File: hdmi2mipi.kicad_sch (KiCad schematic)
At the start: 168 parts, among them J10 BOOT, J11 USB_C_Receptacle_USB2.0, J2 HDMI_A_1.4, J4 TOUCH, J5 QWIIC, J7 SWD, J8 AudioJack3, J9 QWIIC, Q1 BC846, Q2 BC846, Q3 BC846, Q4 BC846, Q5 BC846, Q6 BC846, Q7 2SC2712, U1 RP2040, U2 W25Q16JVUXIQ, U3 SY6280AAC, U3 W25Q16JVUXIQ, U4 PCA9306DC, U4 SY8079AAC, U8 MS4344, X2 SG-210STF, Y1 12MHz

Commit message: Simplify and get ready for component placement and routing
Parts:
- removed C1, C15, C2: 22p, Capacitor_SMD:C_0402_1005Metric, symbol mch2021-rescue:C-Device
- removed C10, C11, C12, C13, C14, C4, C5, C6, C7: 100n, Capacitor_SMD:C_0402_1005Metric, symbol mch2021-rescue:C-Device
- removed C16, C17, C8: 22u, Capacitor_SMD:C_0805_2012Metric, symbol mch2021-rescue:C-Device
- removed C3, C9: 1u, Capacitor_SMD:C_0402_1005Metric, symbol mch2021-rescue:C-Device
- removed C53: 2.2u, Capacitor_SMD:C_0402_1005Metric, symbol Device:C_Small
- removed C54: ~, Capacitor_SMD:C_0402_1005Metric, symbol Device:C_Small
- removed D2, D3, D4, D5: LED, LED_SMD:LED_0603_1608Metric, symbol Device:LED
- removed D5: D, symbol Device:D
- removed J10: BOOT, Connector_PinHeader_2.54mm:PinHeader_1x02_P2.54mm_Vertical, symbol Connector_Generic:Conn_01x02
- removed J11: USB_C_Receptacle_USB2.0, Connector_USB:USB_C_Receptacle_HRO_TYPE-C-31-M-12, symbol Connector:USB_C_Receptacle_USB2.0
- removed J4: TOUCH, Connector_JST:JST_SH_SM07B-SRSS-TB_1x07-1MP_P1.00mm_Horizontal, symbol Connector_Generic_MountingPin:Conn_01x07_MountingPin
- removed J5: QWIIC, Connector_JST:JST_SH_SM04B-SRSS-TB_1x04-1MP_P1.00mm_Horizontal, symbol Connector_Generic_MountingPin:Conn_01x04_MountingPin
- removed J7: SWD, Connector_JST:JST_SH_SM03B-SRSS-TB_1x03-1MP_P1.00mm_Horizontal, symbol Connector_Generic_MountingPin:Conn_01x03_MountingPin
- removed L1: 2.2u, custom:Inductor_MSC20FC, symbol mch2021-rescue:L-Device
- removed L5: ~, symbol mch2021-rescue:L-Device
- removed R1, R50: 10k, Resistor_SMD:R_0402_1005Metric, symbol Device:R_Small
- removed R14, R15: 5.1k, Resistor_SMD:R_0402_1005Metric, symbol mch2021-rescue:R-Device
- removed R16 (x4): 10k, Resistor_SMD:R_0402_1005Metric, symbol mch2021-rescue:R-Device
- removed R17: 45.3k, Resistor_SMD:R_0402_1005Metric, symbol mch2021-rescue:R-Device
- removed R18, R5, R8: 1k, Resistor_SMD:R_0402_1005Metric, symbol mch2021-rescue:R-Device
- removed R2: 0, Resistor_SMD:R_0402_1005Metric, symbol mch2021-rescue:R-Device
- removed R23, R24, R25, R26, R28: 4.7k, Resistor_SMD:R_0402_1005Metric, symbol Device:R_Small
- removed R3, R4: 10, Resistor_SMD:R_0402_1005Metric, symbol mch2021-rescue:R-Device
- removed R5: 6.8k, Resistor_SMD:R_0402_1005Metric, symbol mch2021-rescue:R-Device
- removed R5 (x2): 100, Resistor_SMD:R_0402_1005Metric, symbol mch2021-rescue:R-Device
- removed R6, R7: 27, Resistor_SMD:R_0402_1005Metric, symbol mch2021-rescue:R_Small-Device
- removed R63: 47k, Resistor_SMD:R_0402_1005Metric, symbol mch2021-rescue:R-Device
- removed R64: 100k, Resistor_SMD:R_0402_1005Metric, symbol mch2021-rescue:R-Device
- removed RN1: 1K, Resistor_SMD:R_Array_Convex_4x0402, symbol Device:R_Pack04
- removed TP1, TP2, TP3: TestPoint, TestPoint:TestPoint_Pad_D1.0mm, symbol Connector:TestPoint
- removed TP4, TP5: TestPoint, TestPoint:TestPoint_Pad_D2.0mm, symbol Connector:TestPoint
- removed U1: RP2040, custom:QFN40P700X700X90-57N, symbol RP2040:RP2040
- removed U12: ~, Package_TO_SOT_SMD:SOT-23-6, symbol lp3382s:LP3382S
- removed U2: W25Q16JVUXIQ, custom:PSON50P300X200X60-9N, symbol mch2021-rescue:SPIFLASH_QSPI-spiflash
- removed U3: W25Q16JVUXIQ, Package_SO:SOIC-8_5.23x5.23mm_P1.27mm, symbol mch2021-rescue:SPIFLASH_QSPI-spiflash
- removed U3: SY6280AAC, Package_TO_SOT_SMD:SOT-23-5, symbol symbols:AAT4610BIGV-1-T1-Power_Management
- removed U4: PCA9306DC, Package_SO:VSSOP-8_2.3x2mm_P0.5mm, symbol Interface:PCA9306DC
- removed U4: SY8079AAC, Package_TO_SOT_SMD:SOT-23-5, symbol mch2021-rescue:TLV62568DBV-Regulator_Switching
- removed Y1: 12MHz, Crystal:Crystal_SMD_3225-4Pin_3.2x2.5mm, symbol mch2021-rescue:Crystal_GND24_Small-Device
- added J1: IO, Connector_PinHeader_2.54mm:PinHeader_2x06_P2.54mm_Vertical, symbol Connector_Generic:Conn_02x06_Odd_Even
- added J4, J5: Conn_01x04, Connector_PinHeader_2.54mm:PinHeader_1x04_P2.54mm_Vertical, symbol Connector_Generic:Conn_01x04
- added J6: Conn_01x03, Connector_PinHeader_2.54mm:PinHeader_1x04_P2.54mm_Vertical, symbol Connector_Generic:Conn_01x03
- C6: value ~ -> 0.1u
- H1, H2, H3, H4: LCSC (none) -> -
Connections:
- net 1V1_EN is gone; now on net +3V3: U4.1 (EN)
- net 1V2_EN is gone; now on net +3V3: U4.1 (EN)
- net 1V8_EN is gone; now on net +3V3: U4.1 (EN)
- net VBUS is gone; now on net +3V3: C6.1, C6.1, C6.1, C8.1, C8.1, C8.1, U4.4 (VIN), U4.4 (VIN), U4.4 (VIN)
- net VDD33_HDMI is gone; now on net +3V3: C6.1, C6.1, C8.1, J3.24 (3.3v), J3.25 (3.3v), Q7.3 (C), R10.2, R27.1, R29.1, R41.1, R43.1, U2.B1 (VDD33_HDMI), U2.G1 (VDD33_HDMI), U2.H2 (VDDIO33), U2.J7 (VDDIO18), X2.1 (~{ST}), X2.4 (Vcc)
- net +1V1: now also J4.2 (Pin_2)
- net +1V2: now also J4.3 (Pin_3)
- net +1V8: now also J4.4 (Pin_4)
- net +3V3: now also R38.1, J1.11 (Pin_11), J5.2 (Pin_2)
- net 1V8_S1: now also J1.3 (Pin_3)
- net 1V8_S2: now also J1.5 (Pin_5)
- net 3V3_S1: now also J1.7 (Pin_7)
- net 3V3_S2: now also J1.9 (Pin_9)
- net GND: now also J1.1 (Pin_1), J1.2 (Pin_2), J4.1 (Pin_1), J5.1 (Pin_1), J6.3 (Pin_3); no longer R38.2
- net at R40.1, U2.J3 (INT): now also J6.1 (Pin_1)
- net at J9.3 (Pin_3), R29.2, U2.K3 (I2C_SDA): now also J5.3 (Pin_3)
- net at J9.4 (Pin_4), R27.2, U2.K4 (I2C_SCL): now also J5.4 (Pin_4)
- net at U2.K8 (~{RESET}): now also R38.2, J6.2 (Pin_2); no longer R38.1
- net at J3.5 (FB2), J3.6 (FB2): now also J1.6 (Pin_6)
- net at J3.1 (FB1), J3.2 (FB1): now also J1.4 (Pin_4)
- net at J3.14 (5.8v-VDD): now also J1.12 (Pin_12)
- net at J3.10 (LED+), J3.8 (LED+), J3.9 (LED+): now also J1.8 (Pin_8)
- net at J3.13 (5.8v-VEE): now also J1.10 (Pin_10)
- no-connect marks 14 -> 12
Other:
- note removed: "I2C0 SDA I2C0 SCL"
- note removed: "I2C1 SDA I2C1 SCL"
- note removed: "Place close to chip"
- note removed: "Place close to pin 44"
- note removed: "Place close to pin 45"
- note removed: "SPI0 SCK SPI0 TX SPI0 RX"
- note removed: "SPI1 SCK SPI1 TX SPI1 RX"
- note removed: "UART0 TX UART0 RX UART0 CTS UART0 RTS"
- note removed: "UART1 TX UART1 RX UART1 CTS UART1 RTS"
- company: Nicolai Electronics -> Nicolai Electronics & Badge.Team
- title: HDMI to MIPI converter -> HDMI to MIPI converter (simplified)
- moved on the sheet: R38

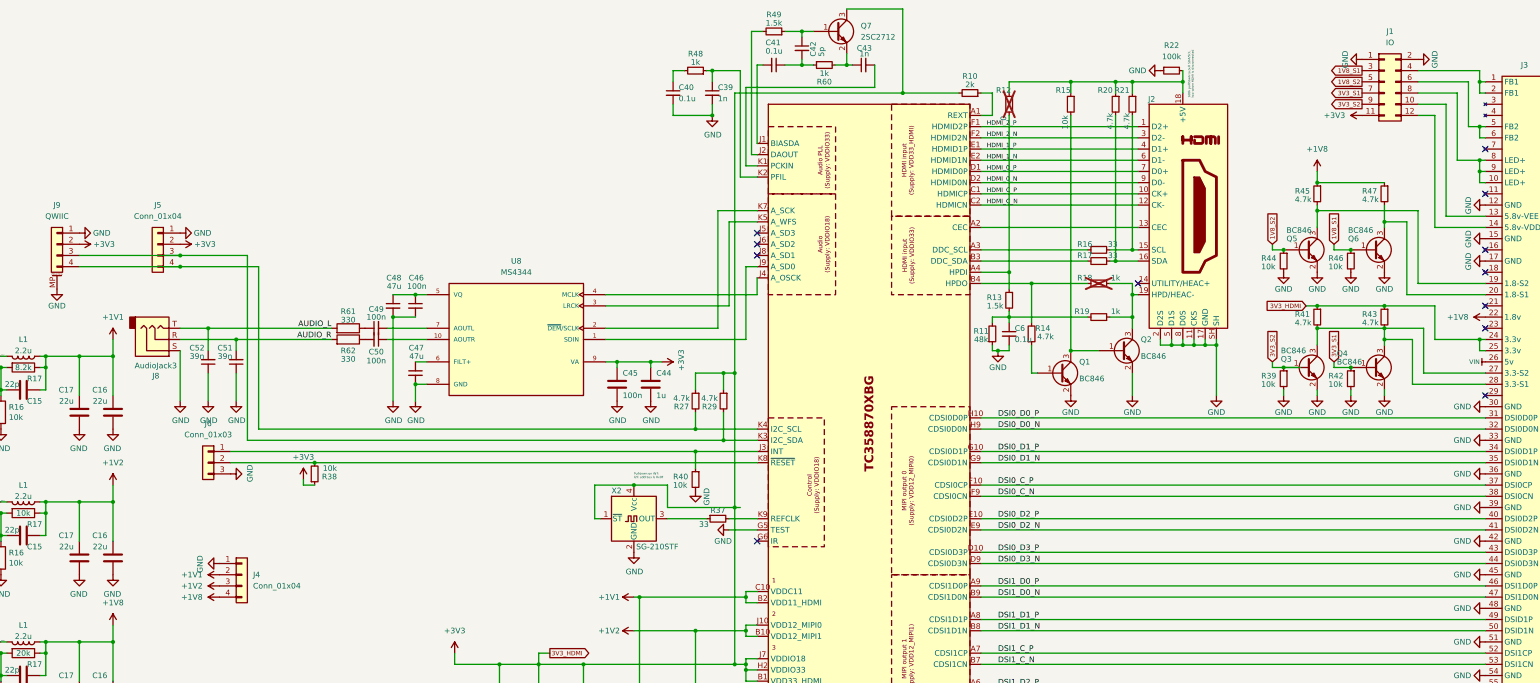
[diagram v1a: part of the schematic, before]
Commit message: Small fixes and combine 2.54mm headers
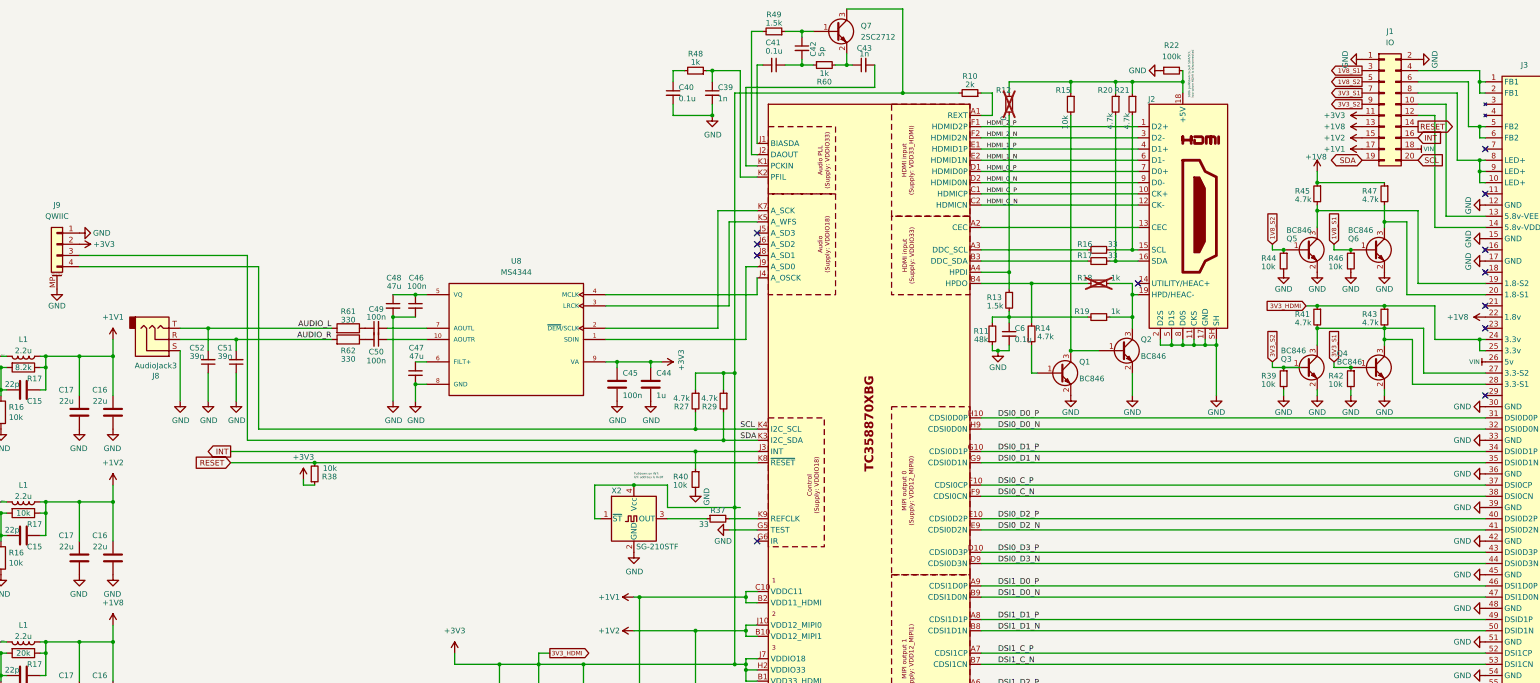
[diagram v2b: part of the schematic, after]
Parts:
- removed J4, J5: Conn_01x04, Connector_PinHeader_2.54mm:PinHeader_1x04_P2.54mm_Vertical, symbol Connector_Generic:Conn_01x04
- removed J6: Conn_01x03, Connector_PinHeader_2.54mm:PinHeader_1x04_P2.54mm_Vertical, symbol Connector_Generic:Conn_01x03
- J1: footprint Connector_PinHeader_2.54mm:PinHeader_2x06_P2.54mm_Vertical -> Connector_PinHeader_2.54mm:PinHeader_2x10_P2.54mm_Vertical; symbol Connector_Generic:Conn_02x06_Odd_Even -> Connector_Generic:Conn_02x10_Odd_Even
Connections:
- net +1V1: now also J1.17 (Pin_17)
- net +1V2: now also J1.15 (Pin_15)
- net +1V8: now also J1.13 (Pin_13)
- net VIN: now also J1.18 (Pin_18)
- net INT: now reaches R40.1, U2.J3 (INT)
- net INT: now also J1.16 (Pin_16)
- net SDA: now reaches J9.3 (Pin_3), R29.2, U2.K3 (I2C_SDA)
- net SDA: now also J1.19 (Pin_19)
- net SCL: now reaches J9.4 (Pin_4), R27.2, U2.K4 (I2C_SCL)
- net SCL: now also J1.20 (Pin_20)
- net RESET: now reaches R38.2, U2.K8 (~{RESET})
- net RESET: now also J1.14 (Pin_14)

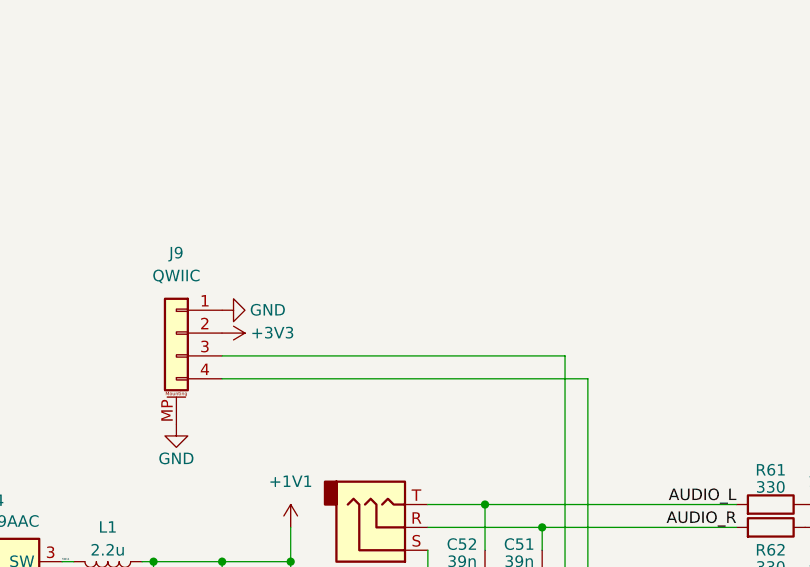
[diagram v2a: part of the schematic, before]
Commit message: Changed copper layers, heaps of other issues.
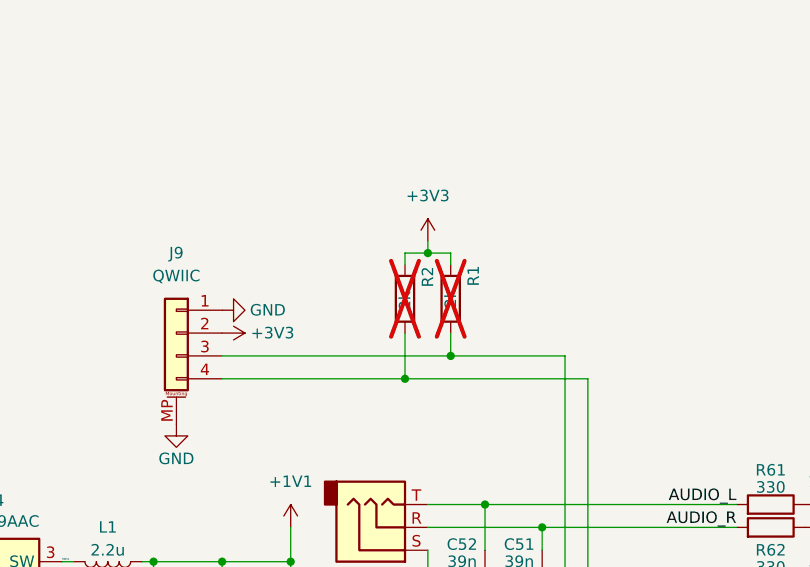
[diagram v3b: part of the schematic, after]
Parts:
- added R1, R2: 2k, Resistor_SMD:R_0402_1005Metric, symbol mch2021-rescue:R-Device
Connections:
- net +3V3: now also R1.1, R2.1
- net SCL: now also R2.2
- net SDA: now also R1.2

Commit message: Last tweaks and order at JLC
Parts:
- C39, C43: LCSC (none) -> C527013
- C40, C41, C6: LCSC (none) -> C106256
- C42: LCSC (none) -> C359289
- H1, H2, H3, H4: now not fitted
- J1: LCSC (none) -> -; now not fitted
- J2: LCSC (none) -> C720616
- J3: LCSC (none) -> C224193
- J9: LCSC (none) -> C160404
- Q1, Q2, Q3, Q4, Q5, Q6: LCSC (none) -> C181138
- Q7: LCSC (none) -> C83447
- R10: LCSC (none) -> C25744
- R11: value 48k -> 47k; LCSC (none) -> C380748
- R12: LCSC (none) -> -
- R13, R49: LCSC (none) -> C409724
- U2: LCSC (none) -> C3008712
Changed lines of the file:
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@@
 	(title_block
 		(title "HDMI to MIPI converter (simplified)")
-		(date "2024-02-21")
+		(date "2024-03-29")
 		(rev "0.1")
 		(company "Nicolai Electronics & Badge.Team")
@@
 			)
 		)
+		(property "LCSC" "C3008712"
+			(at 254 175.26 0)
+			(effects
+				(font
+					(size 1.27 1.27)
+				)
+				(hide yes)
+			)
+		)
 		(pin "H10"
 		)
@@
 		(in_bom yes)
 		(on_board yes)
-		(dnp no)
+		(dnp yes)
 		(fields_autoplaced yes)
 		(property "Reference" "J1"
@@
 			)
 		)
+		(property "LCSC" "-"
+			(at 370.84 102.87 0)
+			(effects
+				(font
+					(size 1.27 1.27)
+				)
+				(hide yes)
+			)
+		)
 		(pin "6"
 		)
@@
 			)
 		)
+		(property "LCSC" "C409724"
+			(at 232.41 86.36 0)
+			(effects
+				(font
+					(size 1.27 1.27)
+				)
+				(hide yes)
+			)
+		)
 		(pin "2"
 		)
@@
 			)
 		)
+		(property "LCSC" "C181138"
+			(at 311.15 158.75 0)
+			(effects
+				(font
+					(size 1.27 1.27)
+				)
+				(hide yes)
+			)
+		)
 		(pin "1"
 		)
@@
 			)
 		)
+		(property "LCSC" "C181138"
+			(at 297.18 163.83 0)
+			(effects
+				(font
+					(size 1.27 1.27)
+				)
+				(hide yes)
+			)
+		)
 		(pin "1"
 		)
@@
 			)
 		)
-		(property "Value" "48k"
+		(property "Value" "47k"
 			(at 279.4 156.21 0)
 			(effects
@@
 			)
 		)
+		(property "LCSC" "C380748"
+			(at 281.94 154.94 0)
+			(effects
+				(font
+					(size 1.27 1.27)
+				)
+				(hide yes)
+			)
+		)
 		(pin "2"
 		)
@@
 			)
 		)
+		(property "LCSC" "C83447"
+			(at 246.38 86.36 0)
+			(effects
+				(font
+					(size 1.27 1.27)
+				)
+				(hide yes)
+			)
+		)
 		(pin "1"
 		)
@@
 			)
 		)
+		(property "LCSC" "C25744"
+			(at 276.86 100.33 0)
+			(effects
+				(font
+					(size 1.27 1.27)
+				)
+				(hide yes)
+			)
+		)
 		(pin "2"
 		)
@@
 			)
 		)
+		(property "LCSC" "C527013"
+			(at 252.73 93.98 0)
+			(effects
+				(font
+					(size 1.27 1.27)
+				)
+				(hide yes)
+			)
+		)
 		(pin "2"
 		)
@@
 			)
 		)
+		(property "LCSC" "C181138"
+			(at 368.3 135.89 0)
+			(effects
+				(font
+					(size 1.27 1.27)
+				)
+				(hide yes)
+			)
+		)
 		(pin "3"
 		)
@@
 			)
 		)
+		(property "LCSC" "C160404"
+			(at 69.85 134.62 0)
+			(effects
+				(font
+					(size 1.27 1.27)
+				)
+				(hide yes)
+			)
+		)
 		(pin "2"
 		)
@@
 			)
 		)
+		(property "LCSC" "C359289"
+			(at 238.76 90.17 0)
+			(effects
+				(font
+					(size 1.27 1.27)
+				)
+				(hide yes)
+			)
+		)
 		(pin "2"
 		)
@@
 			)
 		)
+		(property "LCSC" "C106256"
+			(at 285.75 154.94 0)
+			(effects
+				(font
+					(size 1.27 1.27)
+				)
+				(hide yes)
+			)
+		)
 		(pin "2"
 		)
@@
 		(in_bom yes)
 		(on_board yes)
-		(dnp no)
+		(dnp yes)
 		(property "Reference" "H2"
 			(at 276.86 264.795 0)
@@
 		(in_bom yes)
 		(on_board yes)
-		(dnp no)
+		(dnp yes)
 		(property "Reference" "H3"
 			(at 281.94 264.795 0)
@@
 			)
 		)
+		(property "LCSC" "C106256"
+			(at 232.41 93.98 0)
+			(effects
+				(font
+					(size 1.27 1.27)
+				)
+				(hide yes)
+			)
+		)
 		(pin "2"
 		)
@@
 			)
 		)
+		(property "LCSC" "C224193"
+			(at 398.78 173.99 0)
+			(effects
+				(font
+					(size 1.27 1.27)
+				)
+				(hide yes)
+			)
+		)
 		(pin "34"
 		)
@@
 			)
 		)
+		(property "LCSC" "C720616"
+			(at 325.12 128.27 0)
+			(effects
+				(font
+					(size 1.27 1.27)
+				)
+				(hide yes)
+			)
+		)
 		(pin "7"
 		)
@@
 			)
 		)
+		(property "LCSC" "C527013"
+			(at 218.44 100.33 0)
+			(effects
+				(font
+					(size 1.27 1.27)
+				)
+				(hide yes)
+			)
+		)
 		(pin "2"
 		)
@@
 		(in_bom yes)
 		(on_board yes)
-		(dnp no)
+		(dnp yes)
 		(property "Reference" "H1"
 			(at 271.78 264.795 0)
@@
 			)
 		)
+		(property "LCSC" "C181138"
+			(at 353.06 162.56 0)
+			(effects
+				(font
+					(size 1.27 1.27)
+				)
+				(hide yes)
+			)
+		)
 		(pin "3"
 		)
@@
 			)
 		)
+		(property "LCSC" "C409724"
+			(at 285.75 147.32 0)
+			(effects
+				(font
+					(size 1.27 1.27)
+				)
+				(hide yes)
+			)
+		)
 		(pin "2"
 		)
@@
 		(in_bom yes)
 		(on_board yes)
-		(dnp no)
+		(dnp yes)
 		(property "Reference" "H4"
 			(at 287.02 264.795 0)
@@
 			)
 		)
+		(property "LCSC" "C181138"
+			(at 368.3 162.56 0)
+			(effects
+				(font
+					(size 1.27 1.27)
+				)
+				(hide yes)
+			)
+		)
 		(pin "3"
 		)
@@
 			)
 		)
+		(property "LCSC" "-"
+			(at 285.75 102.87 0)
+			(effects
+				(font
+					(size 1.27 1.27)
+				)
+				(hide yes)
+			)
+		)
 		(pin "2"
 		)
@@
 			)
 		)
+		(property "LCSC" "C106256"
+			(at 209.55 100.33 0)
+			(effects
+				(font
+					(size 1.27 1.27)
+				)
+				(hide yes)
+			)
+		)
 		(pin "2"
 		)
@@
 			(at 353.06 135.89 0)
 			(effects
+				(font
+					(size 1.27 1.27)
+				)
+				(hide yes)
+			)
+		)
+		(property "LCSC" "C181138"
+			(at 353.06 135.89 0)
+			(effects
